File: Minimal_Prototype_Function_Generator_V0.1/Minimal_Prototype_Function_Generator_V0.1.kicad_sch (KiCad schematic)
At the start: 3 parts, among them J6 142-0701-201

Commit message: Updated schemattic documentation
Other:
- note added: "- Fixed resistor divider values (Were reversed order and above 5 volt values were off)"
- note added: "- Initial Setup"
- note added: "- SPI Cs rename, and not routed to sensors. We could use GPIO for this - New MFR# for M2 stubs - Seperated stubs from M.2 footprint - ADC and INT to comm module - Placed test points closer to edge"
- note added: "- Solved issue with resistor divider - Setup Schematic documentation - Setup DRC rules"
- note added: "- Updated 3d models for M.2 and SWD Connectors"
- note added: "- Updated connectors to M-key - Update so that sensors have 3 gpio (New pinout for MCU!) - Cleaned the schematic - Complete reroute"
- note added: "- Updated hole location"
- note added: "11/02/2025"
- note added: "13/02/2025"
- note added: "14/04/2025"
- note added: "18/6/2025"
- note added: "20/02/2025"
- note added: "21/03/2025"
- note added: "22/01/2025"
- note added: "25/02/2025"
- note added: "3.0"
- note added: "3.0.1"
- note added: "4A Max, 1A max per module For 1 oz copper (35 µm thickness) PCB traces at a 10°C temperature rise: External traces carry approximately 2.2A (0.4mm), 2.6A (0.5mm), 3.0A (0.6mm), 3.4A (0.7mm), 3.8A (0.8mm), and 4.2A (0.9mm). Internal traces carry approximately 1.2A (0.4mm), 1.5A (0.5mm), 1.8A (0.6mm), 2.1A (0.7mm), 2.4A (0.8mm), and 2.7A (0.9mm). For 2 oz copper (70 µm thickness) PCB traces at a 10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"
- note added: "Board thickness: 1.6mm Impedance match: No Base material: Default Color: Default Outer copper Weight: Default Gold fingers: No Castellated holes: No Edge plating: No"
- note added: "Changelog"
- note added: "Date"
- note added: "Jop"
- note added: "Marlo"
- note added: "Module details"
- note added: "Name"
- note added: "Ordered"
- note added: "Ordering specifications"
- note added: "Updates"
- note added: "Version"
- note added: "Victor"

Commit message: Updated PCB and schematic, according to feedback
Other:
- note added: "- Completed schematics"
- note added: "- Initial PCB design, sent for review"
- note added: "- Input voltage: 5V (from USB-C connector) - Expected maximum current consumption: 1500mA - Current rating: 5A? - A couple of testpoints are available for voltage level testing - UART header for debugging - I2C and SPI headers for debugging - Output 1-4 are function generator outputs after amplification - 2 headers for external/internal clock select are available"
- note added: "- Updated PCB component placement - Recalculated impedance parameters for USB diff. pair - Added descriptions to schematics"
- note added: "0.1"
- note added: "05/09/2025"
- note added: "1.0"
- note added: "11/09/2025"
- note added: "15/09/2025"
- note added: "Board thickness: 1.6mm Impedance match: Yes (for USB2.0 differential pair) Base material: Default Color: Default Outer copper Weight: Default Gold fingers: No Castellated holes: No Edge plating: No"
- note added: "Ignatijs"
- note added: "pre-0.1"
- note removed: "- Fixed resistor divider values (Were reversed order and above 5 volt values were off)"
- note removed: "- Initial Setup"
- note removed: "- SPI Cs rename, and not routed to sensors. We could use GPIO for this - New MFR# for M2 stubs - Seperated stubs from M.2 footprint - ADC and INT to comm module - Placed test points closer to edge"
- note removed: "- Solved issue with resistor divider - Setup Schematic documentation - Setup DRC rules"
- note removed: "- Updated 3d models for M.2 and SWD Connectors"
- note removed: "- Updated connectors to M-key - Update so that sensors have 3 gpio (New pinout for MCU!) - Cleaned the schematic - Complete reroute"
- note removed: "- Updated hole location"
- note removed: "11/02/2025"
- note removed: "13/02/2025"
- note removed: "14/04/2025"
- note removed: "18/6/2025"
- note removed: "20/02/2025"
- note removed: "21/03/2025"
- note removed: "22/01/2025"
- note removed: "25/02/2025"
- note removed: "3.0"
- note removed: "3.0.1"
- note removed: "4A Max, 1A max per module For 1 oz copper (35 µm thickness) PCB traces at a 10°C temperature rise: External traces carry approximately 2.2A (0.4mm), 2.6A (0.5mm), 3.0A (0.6mm), 3.4A (0.7mm), 3.8A (0.8mm), and 4.2A (0.9mm). Internal traces carry approximately 1.2A (0.4mm), 1.5A (0.5mm), 1.8A (0.6mm), 2.1A (0.7mm), 2.4A (0.8mm), and 2.7A (0.9mm). For 2 oz copper (70 µm thickness) PCB traces at a 10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"
- note removed: "Board thickness: 1.6mm Impedance match: No Base material: Default Color: Default Outer copper Weight: Default Gold fingers: No Castellated holes: No Edge plating: No"
- note removed: "Marlo"
- note removed: "Ordered"
- note removed: "Victor"
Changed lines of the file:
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@@
 		)
 	)
-	(text "Jop"
-		(exclude_from_sim no)
-		(at 452.374 110.4157 0)
-		(effects
-			(font
-				(size 2.54 2.54)
-			)
-		)
-	)
-	(text "25/02/2025"
-		(exclude_from_sim no)
-		(at 482.346 93.1437 0)
-		(effects
-			(font
-				(size 2.54 2.54)
-			)
-		)
-	)
-	(text "Ordered"
-		(exclude_from_sim no)
-		(at 582.168 128.27 0)
-		(effects
-			(font
-				(size 1.524 1.524)
-			)
-		)
-	)
-	(text "4A Max, 1A max per module\n\n\n\n\n\nFor 1 oz copper (35 µm thickness) PCB traces at a 10°C temperature rise:\n\nExternal traces carry approximately 2.2A (0.4mm), 2.6A (0.5mm), 3.0A (0.6mm), 3.4A (0.7mm), 3.8A (0.8mm), and 4.2A (0.9mm).\nInternal traces carry approximately 1.2A (0.4mm), 1.5A (0.5mm), 1.8A (0.6mm), 2.1A (0.7mm), 2.4A (0.8mm), and 2.7A (0.9mm).\nFor 2 oz copper (70 µm thickness) PCB traces at a 10°C temperature rise:\n\nExternal traces carry approximately 4.0A (0.4mm), 4.7A (0.5mm), 5.5A (0.6mm), 6.2A (0.7mm), 7.0A (0.8mm), and 7.7A (0.9mm).\nInternal traces carry approximately 2.1A (0.4mm), 2.6A (0.5mm), 3.1A (0.6mm), 3.6A (0.7mm), 4.1A (0.8mm), and 4.6A (0.9mm)."
-		(exclude_from_sim no)
-		(at 892.81 19.4837 0)
-		(effects
-			(font
-				(size 1.27 1.27)
-			)
-		)
-	)
-	(text "18/6/2025"
-		(exclude_from_sim no)
-		(at 482.092 147.4997 0)
-		(effects
-			(font
-				(size 2.54 2.54)
-			)
-		)
-	)
-	(text "22/01/2025"
-		(exclude_from_sim no)
-		(at 483.108 19.2297 0)
-		(effects
-			(font
-				(size 2.54 2.54)
-			)
-		)
-	)
-	(text "- Updated 3d models for M.2 and SWD Connectors"
-		(exclude_from_sim no)
-		(at 588.772 92.6357 0)
-		(effects
-			(font
-				(size 2.54 2.54)
-			)
-		)
-	)
-	(text "3.0"
-		(exclude_from_sim no)
-		(at 515.874 19.7377 0)
+	(text "1.0"
+		(exclude_from_sim no)
+		(at 514.604 57.658 0)
+		(effects
+			(font
+				(size 2.54 2.54)
+			)
+		)
+	)
+	(text "- Updated PCB component placement\n- Recalculated impedance parameters for USB diff. pair\n- Added descriptions to schematics"
+		(exclude_from_sim no)
+		(at 534.924 56.896 0)
+		(effects
+			(font
+				(size 2.54 2.54)
+			)
+			(justify left)
+		)
+	)
+	(text "- Input voltage: 5V (from USB-C connector)\n- Expected maximum current consumption: 1500mA\n- Current rating: 5A?\n- A couple of testpoints are available for voltage level testing\n- UART header for debugging\n- I2C and SPI headers for debugging\n- Output 1-4 are function generator outputs after amplification\n- 2 headers for external/internal clock select are available\n"
+		(exclude_from_sim no)
+		(at 826.262 16.764 0)
+		(effects
+			(font
+				(size 1.27 1.27)
+			)
+			(justify left)
+		)
+	)
+	(text "05/09/2025"
+		(exclude_from_sim no)
+		(at 482.854 21.844 0)
+		(effects
+			(font
+				(size 2.54 2.54)
+			)
+		)
+	)
+	(text "pre-0.1"
+		(exclude_from_sim no)
+		(at 514.604 21.336 0)
 		(effects
 			(font
@@
 		)
 	)
-	(text "- Fixed resistor divider values \n  (Were reversed order and above 5 volt values were off)"
-		(exclude_from_sim no)
-		(at 539.877 56.6947 0)
-		(effects
-			(font
-				(size 2.54 2.54)
-			)
-			(justify left)
+	(text "11/09/2025"
+		(exclude_from_sim no)
+		(at 482.346 40.386 0)
+		(effects
+			(font
+				(size 2.54 2.54)
+			)
 		)
 	)
@@
 		)
 	)
-	(text "- SPI Cs rename, and not routed to sensors. We could use GPIO for this\n- New MFR# for M2 stubs\n- Seperated stubs from M.2 footprint\n- ADC and INT to comm module\n- Placed test points closer to edge"
-		(exclude_from_sim no)
-		(at 582.422 110.4157 0)
-		(effects
-			(font
-				(size 1.524 1.524)
-			)
-		)
-	)
-	(text "- Initial Setup"
-		(exclude_from_sim no)
-		(at 554.482 19.4837 0)
-		(effects
-			(font
-				(size 2.54 2.54)
-			)
-		)
-	)
-	(text "Jop"
-		(exclude_from_sim no)
-		(at 452.12 128.27 0)
-		(effects
-			(font
-				(size 2.54 2.54)
-			)
-		)
-	)
-	(text "11/02/2025"
-		(exclude_from_sim no)
-		(at 482.473 39.6767 0)
-		(effects
-			(font
-				(size 2.54 2.54)
-			)
-		)
-	)
-	(text "21/03/2025"
-		(exclude_from_sim no)
-		(at 482.346 110.9237 0)
-		(effects
-			(font
-				(size 2.54 2.54)
-			)
-		)
-	)
-	(text "3.0"
-		(exclude_from_sim no)
-		(at 514.096 93.3977 0)
-		(effects
-			(font
-				(size 2.54 2.54)
-			)
-		)
-	)
-	(text "14/04/2025"
-		(exclude_from_sim no)
-		(at 482.092 128.778 0)
-		(effects
-			(font
-				(size 2.54 2.54)
-			)
-		)
-	)
-	(text "- Solved issue with resistor divider\n- Setup Schematic documentation\n- Setup DRC rules"
-		(exclude_from_sim no)
-		(at 539.877 40.1847 0)
+	(text "Ignatijs"
+		(exclude_from_sim no)
+		(at 452.374 57.658 0)
+		(effects
+			(font
+				(size 2.54 2.54)
+			)
+		)
+	)
+	(text "- Completed schematics"
+		(exclude_from_sim no)
+		(at 534.416 17.272 0)
+		(effects
+			(font
+				(size 2.54 2.54)
+			)
+			(justify left)
+		)
+	)
+	(text "- Initial PCB design, sent for review"
+		(exclude_from_sim no)
+		(at 535.432 36.068 0)
 		(effects
 			(font
@@
 			(font
 				(size 5.08 5.08)
-			)
-		)
-	)
-	(text "3.0"
-		(exclude_from_sim no)
-		(at 513.9067 75.9008 0)
-		(effects
-			(font
-				(size 2.54 2.54)
-			)
-		)
-	)
-	(text "Victor"
-		(exclude_from_sim no)
-		(at 452.374 92.6357 0)
-		(effects
-			(font
-				(size 2.54 2.54)
 			)
 		)
@@
 		)
 	)
-	(text "20/02/2025"
-		(exclude_from_sim no)
-		(at 482.4107 75.6468 0)
-		(effects
-			(font
-				(size 2.54 2.54)
-			)
-		)
-	)
-	(text "- Updated hole location"
-		(exclude_from_sim no)
-		(at 548.894 140.8957 0)
-		(effects
-			(font
-				(size 1.524 1.524)
-			)
-		)
-	)
 	(text "Changelog"
 		(exclude_from_sim no)
@@
 		)
 	)
-	(text "3.0.1"
-		(exclude_from_sim no)
-		(at 513.842 129.032 0)
-		(effects
-			(font
-				(size 2.54 2.54)
-			)
-		)
-	)
 	(text "5V Input to 3v3 Conversion"
 		(exclude_from_sim no)
@@
 		)
 	)
-	(text "3.0"
-		(exclude_from_sim no)
-		(at 514.477 40.1847 0)
-		(effects
-			(font
-				(size 2.54 2.54)
-			)
-		)
-	)
-	(text "- Updated connectors to M-key\n- Update so that sensors have 3 gpio (New pinout for MCU!)\n- Cleaned the schematic\n- Complete reroute"
-		(exclude_from_sim no)
-		(at 539.8147 74.6308 0)
-		(effects
-			(font
-				(size 2.54 2.54)
-			)
-			(justify left)
+	(text "0.1"
+		(exclude_from_sim no)
+		(at 514.096 39.878 0)
+		(effects
+			(font
+				(size 2.54 2.54)
+			)
+		)
+	)
+	(text "15/09/2025"
+		(exclude_from_sim no)
+		(at 482.854 58.166 0)
+		(effects
+			(font
+				(size 2.54 2.54)
+			)
 		)
 	)
@@
 		)
 	)
-	(text "Marlo"
-		(exclude_from_sim no)
-		(at 453.136 18.7217 0)
-		(effects
-			(font
-				(size 2.54 2.54)
-			)
-		)
-	)
-	(text "Marlo"
-		(exclude_from_sim no)
-		(at 452.12 146.9917 0)
-		(effects
-			(font
-				(size 2.54 2.54)
-			)
-		)
-	)
-	(text "3.0"
-		(exclude_from_sim no)
-		(at 513.969 57.9647 0)
+	(text "Jop"
+		(exclude_from_sim no)
+		(at 452.374 21.336 0)
 		(effects
 			(font
@@
 		)
 	)
-	(text "13/02/2025"
-		(exclude_from_sim no)
-		(at 482.473 57.7107 0)
-		(effects
-			(font
-				(size 2.54 2.54)
-			)
-		)
-	)
-	(text "Marlo"
-		(exclude_from_sim no)
-		(at 452.501 58.7267 0)
-		(effects
-			(font
-				(size 2.54 2.54)
-			)
-		)
-	)
-	(text "3.0.1"
-		(exclude_from_sim no)
-		(at 513.842 147.7537 0)
-		(effects
-			(font
-				(size 2.54 2.54)
-			)
-		)
-	)
-	(text "3.0.1"
-		(exclude_from_sim no)
-		(at 514.096 111.1777 0)
-		(effects
-			(font
-				(size 2.54 2.54)
-			)
-		)
-	)
-	(text "Jop"
-		(exclude_from_sim no)
-		(at 452.4387 76.6628 0)
-		(effects
-			(font
-				(size 2.54 2.54)
-			)
-		)
-	)
 	(text "Not isolated, can be done with an external optical isolator"
 		(exclude_from_sim no)
@@
 		)
 	)
-	(text "Jop"
-		(exclude_from_sim no)
-		(at 451.993 39.1687 0)
-		(effects
-			(font
-				(size 2.54 2.54)
-			)
-		)
-	)
-	(text "Board thickness: 1.6mm\nImpedance match: No\nBase material: Default\nColor: Default\nOuter copper Weight: Default\nGold fingers: No\nCastellated holes: No\nEdge plating: No"
+	(text "Board thickness: 1.6mm\nImpedance match: Yes (for USB2.0 differential pair)\nBase material: Default\nColor: Default\nOuter copper Weight: Default\nGold fingers: No\nCastellated holes: No\nEdge plating: No"
 		(exclude_from_sim no)
 		(at 685.419 23.9287 0)
@@
 		)
 	)
+	(text "Ignatijs"
+		(exclude_from_sim no)
+		(at 451.866 39.878 0)
+		(effects
+			(font
+				(size 2.54 2.54)
+			)
+		)
+	)

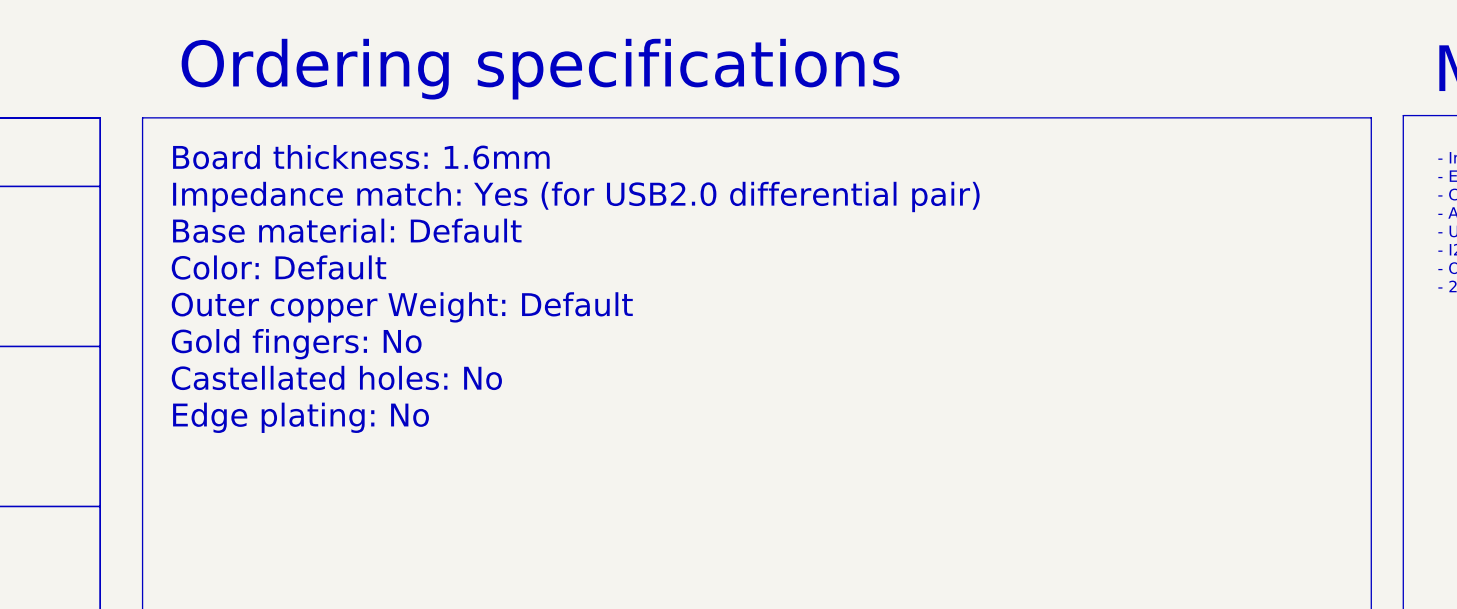
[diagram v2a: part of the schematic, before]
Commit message: Added info on impedance matching
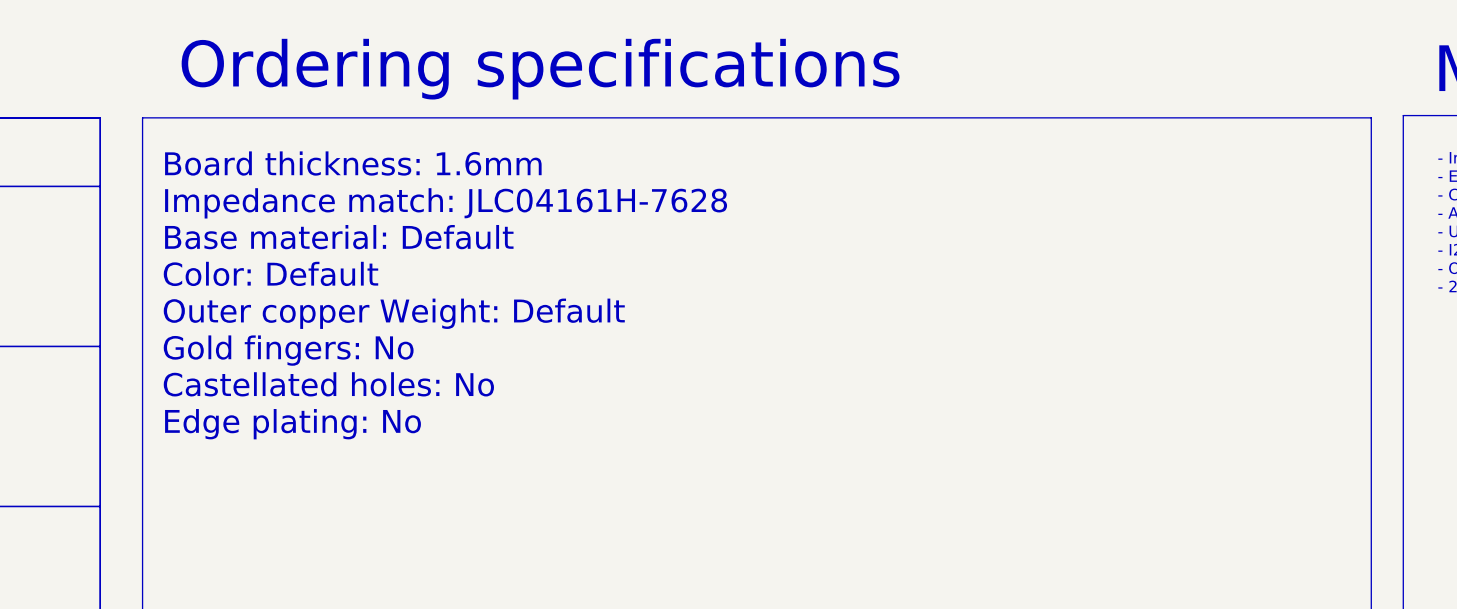
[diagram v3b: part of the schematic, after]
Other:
- note added: "Board thickness: 1.6mm Impedance match: JLC04161H-7628 Base material: Default Color: Default Outer copper Weight: Default Gold fingers: No Castellated holes: No Edge plating: No"
- note removed: "Board thickness: 1.6mm Impedance match: Yes (for USB2.0 differential pair) Base material: Default Color: Default Outer copper Weight: Default Gold fingers: No Castellated holes: No Edge plating: No"

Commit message: Order
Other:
- note added: "- Updated fields for order - Order"
- note added: "29/09/2025"
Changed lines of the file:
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@@
+		)
+	)
+	(text "Ignatijs"
+		(exclude_from_sim no)
+		(at 452.374 74.422 0)
+		(effects
+			(font
+				(size 2.54 2.54)
+			)
 		)
 	)
 	(text "1.0"
 		(exclude_from_sim no)
+		(at 514.604 74.422 0)
+		(effects
+			(font
+				(size 2.54 2.54)
+			)
+		)
+	)
+	(text "1.0"
+		(exclude_from_sim no)
 		(at 514.604 57.658 0)
 		(effects
@@
 			(font
 				(size 5.08 5.08)
+			)
+		)
+	)
+	(text "- Updated fields for order\n- Order"
+		(exclude_from_sim no)
+		(at 534.924 73.66 0)
+		(effects
+			(font
+				(size 2.54 2.54)
+			)
+			(justify left)
+		)
+	)
+	(text "29/09/2025"
+		(exclude_from_sim no)
+		(at 482.854 74.93 0)
+		(effects
+			(font
+				(size 2.54 2.54)
 			)
 		)
@@
 			"r7+3oigAAAAAAGBns634YxX7C1kJAAAAAADAjBwKAAAAAADAMgIKAAAAAADAMgIKAAAAAADAMgIK"
 			"AAAAAADAMgIKAAAAAADAMgIKAAAAAADAMgIKAAAAAADAMgIKAAAAAADAMgIKAAAAAADAsv8HYsf0"
-			"BxDPsAYAAAAASUVORK5CYII="
-		)
-	)
+			"BxDPsAYAAAAASUVORK5CYIIAAAAAAAAAAAAAAAAAAAAAAAAAAAAAAAAAAAAAAAAAAAAAAAAAAAAA"
+			"AAAAAAAAAAAAAAAAAAAAAAAAAAAAAAAAAAAAAAAAAAAAAAAAAAAAAAAAAAAAAAAAAAAAAAAAAAAA"
+			"AAAAAAAAAAAAAAAAAAAAAAAAAAAAAAAAAAAAAAAAAAAAAAAAAAAAAAAAAAAAAAAAAAAAAAAAAAAA"
+			"AAAAAAAAAAAAAAAAAAAAAAAAAAAAAAAAAAAAAAAAAAAAAAAAAAAAAAAAAAAAAAAAAAAAAAAAAAAA"
+			"AAAAAAAAAAAAAAAAAAAAAAAAAAAAAAAAAAAAAAAAAAAAAAAAAAAAAAAAAAAAAAAAAAAAAAAAAAAA"
+			"AAAAAAAAAAAAAAAAAAAAAAAAAAAAAAAAAAAAAAAAAAAAAAAAAAAAAAAAAAAAAAAAAAAAAAAAAAAA"
+			"AAAAAAAAAAAAAAAAAAAAAAAAAAAAAAAAAAAAAAAAAAAAAAAAAAAAAAAAAAAAAAAAAAAAAAAAAAAA"
+			"AAAAAAAAAAAAAAAAAAAAAAAAAAAAAAAAAAAAAAAAAAAAAAAAAAAAAAAAAAAAAAAAAAAAAAAAAAAA"
+			"AAAAAAAAAAAAAAAAAAAAAAAAAAAAAAAAAAAAAAAAAAAAAAAAAAAAAAAAAAAAAAAAAAAAAAAAAAAA"
+			"AAAAAAAAAAAAAAAAAAAAAAAAAAAAAAAAAAAAAAAAAAAAAAAAAAAAAAAAAAAAAAAAAAAAAAAAAAAA"
+			"AAAAAAAAAAAAAAAAAAAAAAAAAAAAAAAAAAAAAAAAAAAAAAAAAAAAAAAAAAAAAAAAAAAAAAAAAAAA"
+			"AAAAAAAAAAAAAAAAAAAAAAAAAAAAAAAAAAAAAAAAAAAAAAAAAAAAAAAAAAAAAAAAAAAAAAAAAAAA"
+			"AAAAAAAAAAAAAAAAAAAAAAAAAAAAAAAAAAAAAAAAAAAAAAAAAAAAAAAAAAAAAAAAAAAAAAAAAAAA"
+			"AAAAAAAAAAAAAAAAAAAAAAAAAAAAAAAAAAAAAAAAAAAAAAAAAAAAAAAAAAAAAAAAAAAAAAAAAAAA"
+			"AAAAAAAAAAAAAAAAAAAAAAAAAAAAAAAAAAAAAAAAAAAAAAAAAAAAAAAAAAAAAAAAAAAAAAAAAAAA"
+			"AAAAAAAAAAAAAAAAAAAAAAAAAAAAAAAAAAAAAAAAAAAAAAAAAAAAAAAAAAAAAAAAAAAAAAAAAAAA"
+			"AAAAAAAAAAAAAAAAAAAAAAAAAAAAAAAAAAAAAAAAAAAAAAAAAAAAAAAAAAAAAAAAAAAAAAAAAAAA"
+			"AAAAAAAAAAAAAAAAAAAAAAAAAAAAAAAAAAAAAAAAAAAAAAAAAAAAAAAAAAAAAAAAAAAAAAAAAAAA"
+			"AAAAAAAAAAAAAAAAAAAAAA=="
+		)
+	)
